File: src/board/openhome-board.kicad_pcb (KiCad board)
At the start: 2 copper layers, 93.1 x 93.1 mm, 10 parts, among them J1 Conn_01x03, J2 Conn_02x11_Odd_Even, J3 Conn_01x04, J4 Conn_01x02, J5 Conn_01x04, K1 G5Q-1, Q1 2N2219

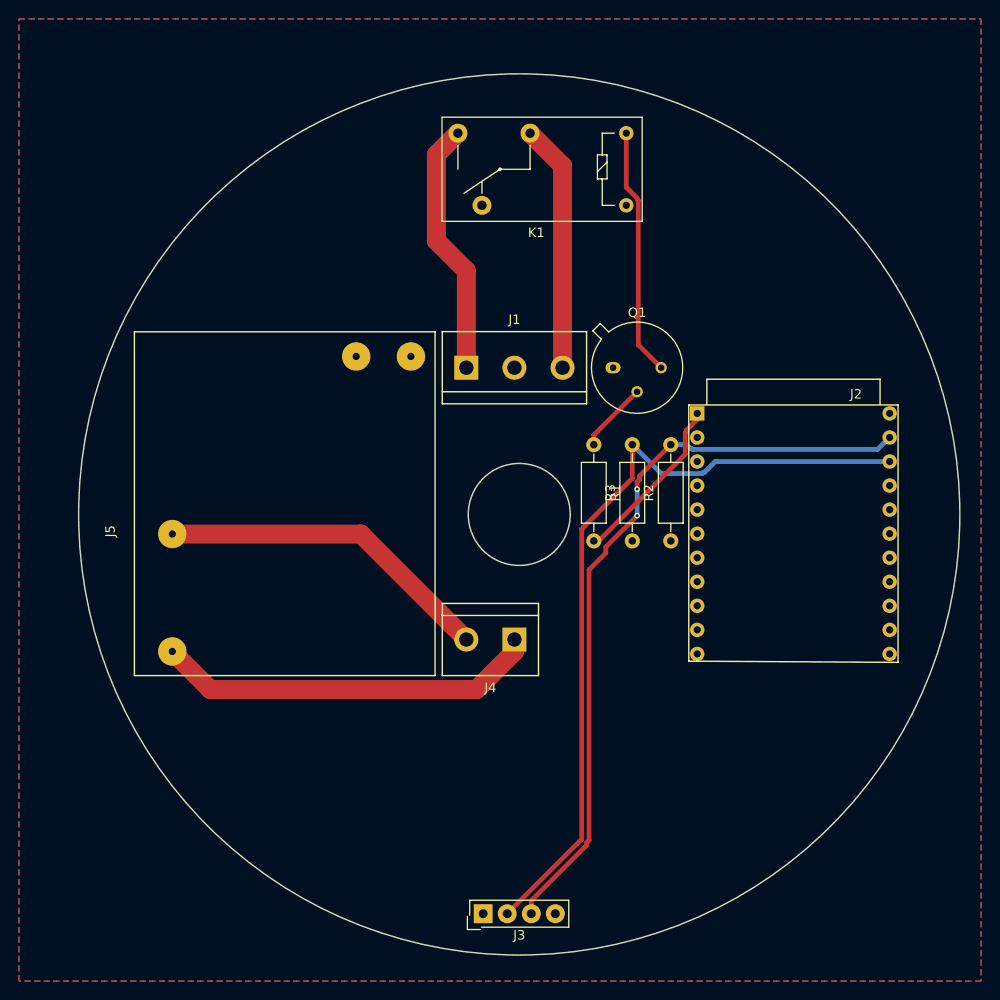
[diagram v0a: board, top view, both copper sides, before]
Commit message: correct some comments + board
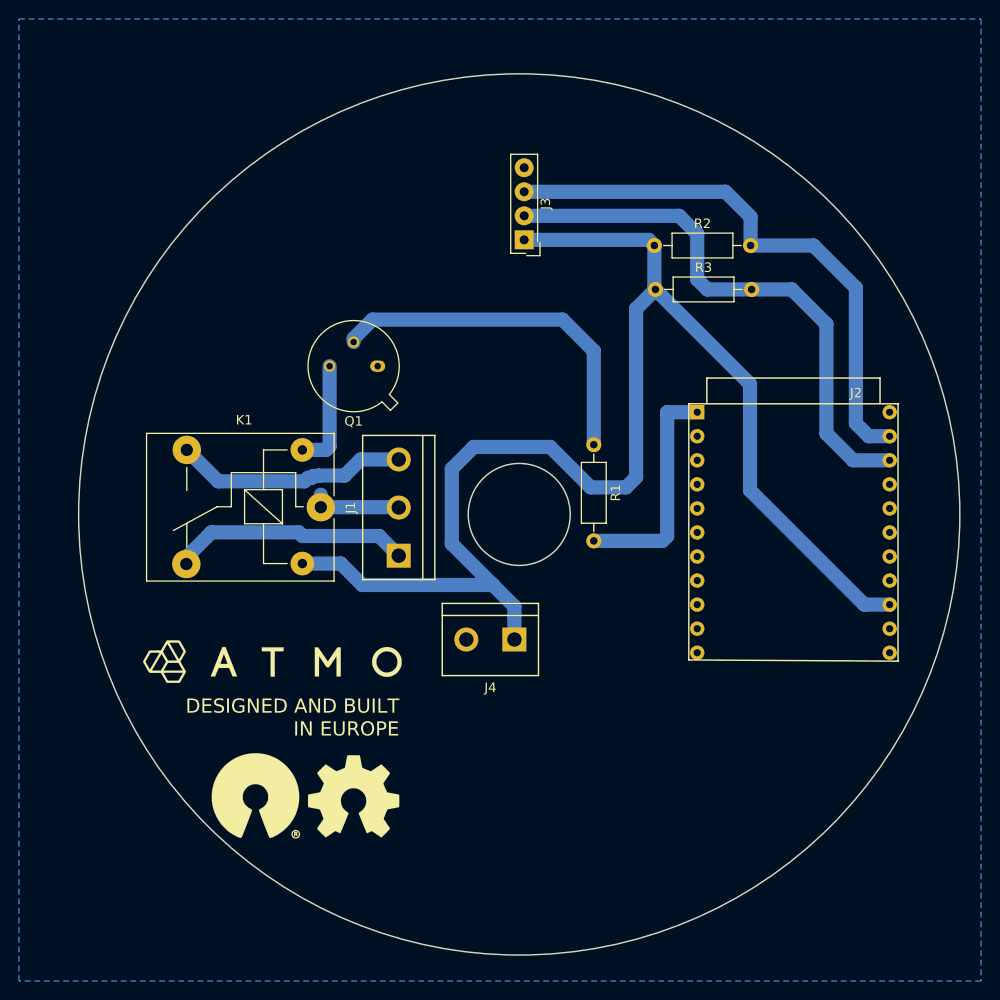
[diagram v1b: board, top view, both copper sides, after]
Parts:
- removed J5: Conn_01x04, atmo:POWER_UNIT
- added ?: , atmo:ATMO-5, F.Cu at (128.4, 105.9)
- added ?: , atmo:OPEN-H, F.Cu at (137.0, 120.3)
- added ?: , atmo:OPEN-S, F.Cu at (126.6, 120.1)
- K1: value G5Q-1 -> SANYOU_SRD_Form_C; footprint Relays_THT:Relay_SPDT_OMRON-G5Q -> Relays_THT:Relay_SPDT_SANYOU_SRD_Series_Form_C
- moved J3 71.3 mm to (155.0, 61.4), turned to 180 degrees
- moved K1 51.0 mm to (133.5, 89.7)
- moved R2 31.2 mm to (168.7, 62.0), turned to 0 degrees
- moved R3 26.7 mm to (168.8, 66.7), turned to 0 degrees
- moved Q1 24.9 mm to (139.5, 74.8), turned to 180 degrees
- moved J1 19.2 mm to (141.7, 89.7), turned to 90 degrees
- moved J2 0.13 mm to (173.2, 79.6)
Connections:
- J4 pad 1: AC_L -> +3V3
- J4 pad 2: AC_N -> GND
- K1 pad 1: Net-(D1-Pad2) -> Net-(J1-Pad2)
- K1 pad 2: Net-(J1-Pad3) -> Net-(D1-Pad2)
- K1 pad 3: Net-(J1-Pad1) -> Net-(J1-Pad3)
- K1 pad 4: Net-(K1-Pad4) -> Net-(J1-Pad1)
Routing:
- net +3V3: track 0.00 -> 148.9 mm
- net AC_L: track 40.8 -> 0.00 mm
- net AC_N: track 35.7 -> 0.00 mm
- net Net-(Q1-Pad2): track 7.48 -> 37.8 mm
- net I2C_THR_SDL: track 84.0 -> 58.9 mm
- net I2C_THR_SDA: track 79.5 -> 59.4 mm, vias 2 -> 0
- net Net-(D1-Pad2): track 26.3 -> 11.5 mm
- net Net-(J1-Pad2): track 0.00 -> 9.57 mm
- net RELAY_DRV: track 18.3 -> 24.2 mm
- net Net-(J1-Pad1): track 28.3 -> 25.2 mm
- net Net-(J1-Pad3): track 26.2 -> 24.7 mm
- removed copper zone on F.Cu, net +3V3
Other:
- net class 2mm: clearance 0.3 -> 0.5; trace_width 2 -> 1.5
- net class Default: clearance 0.2 -> 0.5; trace_width 0.5 -> 1.5
- rule trace_clearance: 0.2 -> 0.5
- board text added: "DESIGNED AND BUILT IN EUROPE"
